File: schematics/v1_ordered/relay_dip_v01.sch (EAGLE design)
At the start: 47 parts, among them IC2 DS2432P

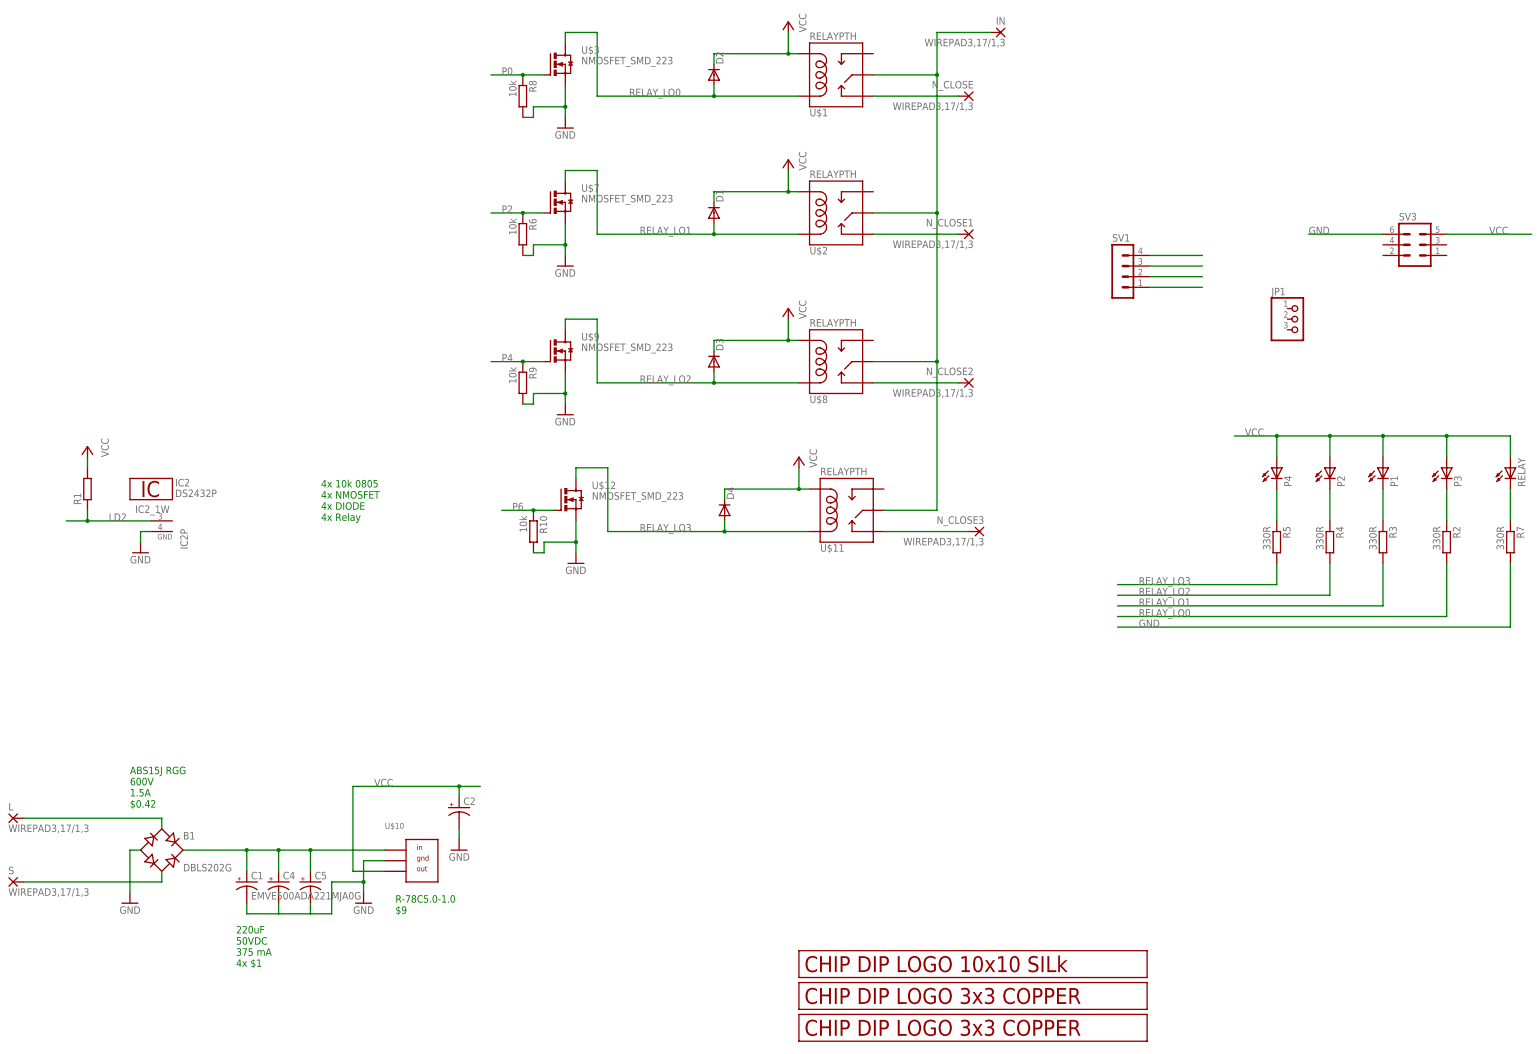
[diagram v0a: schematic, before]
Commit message: moved files to subfolder
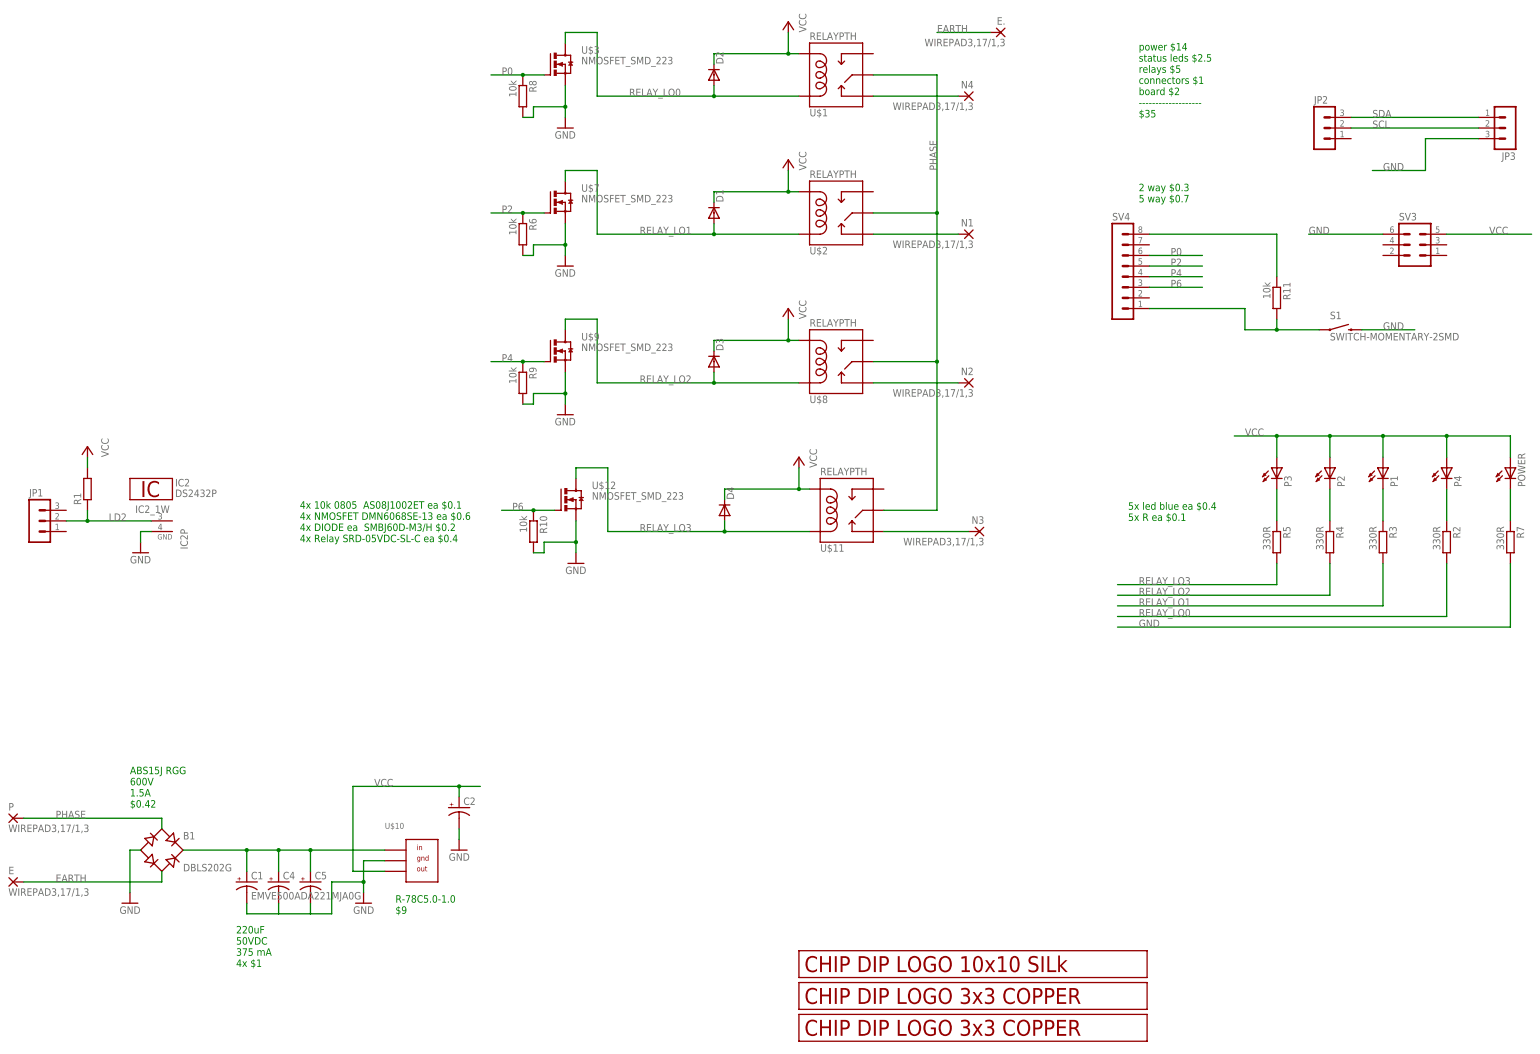
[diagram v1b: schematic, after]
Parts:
- removed SV1: (no value), con-lstb:MA04-1
- added JP2, JP3: (no value), con-lstb:MA03-1
- added R11: 10k, rcl:R-EU_R0805
- added S1: SWITCH-MOMENTARY-2SMD, SparkFun-Electromechanical:SWITCH-MOMENTARY-2SMD
- added SV4: (no value), con-lstb:MA08-1
- JP1: device adafruit:PINHD-1X3 -> con-lstb:MA03-1
- renumbered IN to E., L to P, N_CLOSE to N4, N_CLOSE1 to N1, N_CLOSE2 to N2, N_CLOSE3 to N3, RELAY to POWER, S to E
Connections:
- removed net N$2: B1.AC1, P.P
- removed net RIN: E..P, U$1.SWCOMMON, U$11.SWCOMMON, U$2.SWCOMMON, U$8.SWCOMMON
- new net EARTH: B1.AC2, E..P, E.P
- new net N$1: R11.2, S1.1, SV4.1
- new net PHASE: B1.AC1, P.P, U$1.SWCOMMON, U$11.SWCOMMON, U$2.SWCOMMON, U$8.SWCOMMON
- new net SCL: JP2.2, JP3.2
- new net SDA: JP2.3, JP3.1
- net GND: now also JP3.3, S1.2
- net LD2: now also JP1.2
- net N$10: now also P3.C; no longer P4.C
- net N$3: now also P4.C; no longer P3.C
- net N$6: now also R11.1, SV4.8; no longer B1.AC2, E.P
- net P0: now also SV4.6; no longer SV1.4
- net P2: now also SV4.5; no longer SV1.3
- net P4: now also SV4.4; no longer SV1.2
- net P6: now also SV4.3; no longer SV1.1
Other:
- note added: "2 way $0.3 5 way $0.7"
- note added: "4x 10k 0805 AS08J1002ET ea $0.1 4x NMOSFET DMN6068SE-13 ea $0.6 4x DIODE ea SMBJ60D-M3/H $0.2 4x Relay SRD-05VDC-SL-C ea $0.4"
- note added: "5x led blue ea $0.4 5x R ea $0.1"
- note added: "power $14 status leds $2.5 relays $5 connectors $1 board $2 ------------------- $35"
- note removed: "4x 10k 0805 4x NMOSFET 4x DIODE 4x Relay"
- moved on the sheet: P3, P4

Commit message: v2
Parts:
- removed C1: EMVE500ADA221MJA0G, rcl:CPOL-US150CLZ-0810
- added IC1: 74HCT04D, 74xx-eu:74HCT04D
- C2, C4, C5: value (none) -> EMZR500ADA221MHA0G
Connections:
- removed net N$6: R11.1, SV4.8
- new net 3V: IC1P.VCC, R10.1, R11.1, R6.1, R8.1, R9.1, SV4.8
- new net N$11: IC1E.O, U$12.G
- new net N$2: IC1A.O, U$3.G
- new net N$7: IC1B.O, U$7.G
- new net N$9: IC1C.O, U$9.G
- net GND: now also IC1P.GND; no longer C1.-, R10.2, R6.2, R8.2, R9.2
- net N$5: no longer C1.+
- net P0: now also IC1A.I, R8.2; no longer R8.1, U$3.G
- net P2: now also IC1B.I, R6.2; no longer R6.1, U$7.G
- net P4: now also IC1C.I, R9.2; no longer R9.1, U$9.G
- net P6: now also IC1E.I, R10.2; no longer R10.1, U$12.G
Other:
- note added: "220uF 50VDC 800 mA 4x $0,66 EMZR500ADA221MHA0G"
- note added: "512-DF005S 50V 1.5A $0.446"
- note removed: "220uF 50VDC 375 mA 4x $1"
- note removed: "ABS15J RGG 600V 1.5A $0.42"
- moved on the sheet: R10, R6, R8, R9
